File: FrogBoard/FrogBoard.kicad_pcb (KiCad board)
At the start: 2 copper layers, 59.3 x 50.6 mm, 46 parts, among them J1 Conn_01x10, J10 Conn_01x01, J11 Conn_01x01, J12 Conn_01x02, J13 Conn_01x01, J14 Conn_01x01, J15 Conn_01x01, J2 Conn_01x04, J3 USB_B_Micro, J4 Stickbox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

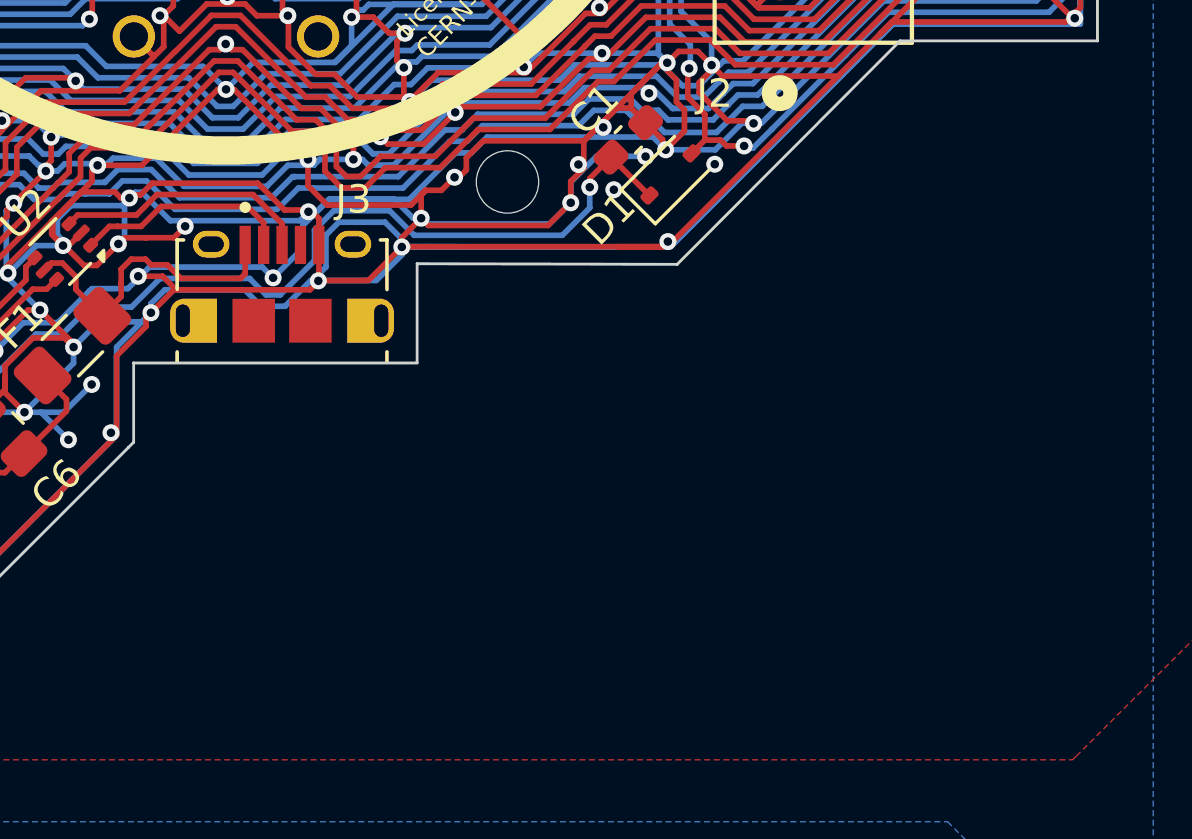
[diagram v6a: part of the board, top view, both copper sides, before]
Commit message: Replace micro B with USB-C connector
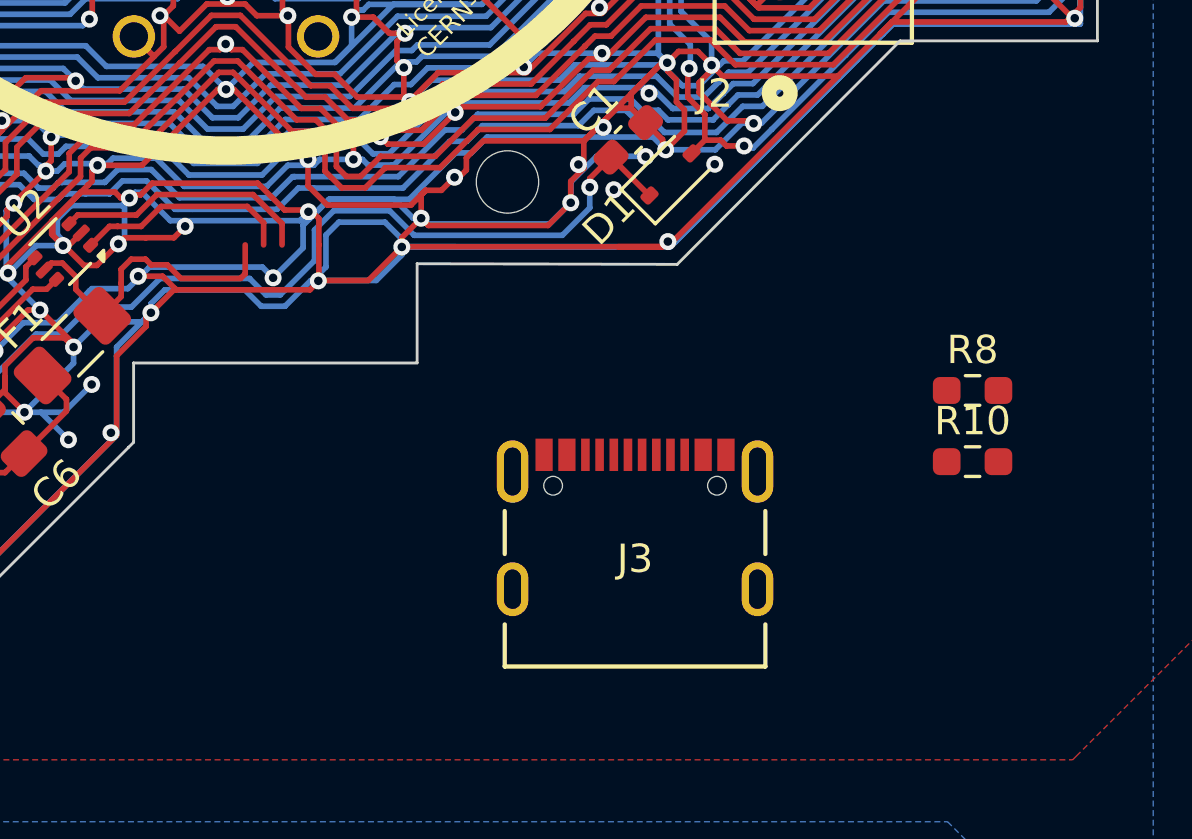
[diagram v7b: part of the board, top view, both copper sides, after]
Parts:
- added R10: 5.1k, Resistor_SMD:R_0603_1608Metric_Pad0.98x0.95mm_HandSolder, F.Cu at (178.1, 117.0)
- added R8: 5.1k, Resistor_SMD:R_0603_1608Metric_Pad0.98x0.95mm_HandSolder, F.Cu at (178.1, 114.5)
- J3: value USB_B_Micro -> USB_C_Receptacle_USB2.0_16P; footprint FrogBoard_footprints:AMPHENOL_10118194-0001LF -> FrogBoard_footprints:CONN16_C16PIN_SHN
- moved J3 15.0 mm to (166.2, 120.4)

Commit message: Cleaned up board edge positions and layed out the main bus
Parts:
- added J16: Conn_01x01, FrogBoard_footprints:FrogBoard_PinHeader_1x01_P1.00mm_Vertical, F.Cu at (21.5, 2.86)
- added J17: Conn_01x01, FrogBoard_footprints:FrogBoard_PinHeader_1x01_P1.00mm_Vertical, F.Cu at (16.8, 3.25)
- added J18: Conn_01x01, FrogBoard_footprints:FrogBoard_PinHeader_1x01_P1.00mm_Vertical, F.Cu at (18.6, 2.85)
- added J19: Conn_01x01, FrogBoard_footprints:FrogBoard_PinHeader_1x01_P1.00mm_Vertical, F.Cu at (29.2, -0.06)
- added J20: Conn_01x01, FrogBoard_footprints:FrogBoard_PinHeader_1x01_P1.00mm_Vertical, F.Cu at (28.5, 10.9)
- added J21: Conn_01x01, FrogBoard_footprints:FrogBoard_PinHeader_1x01_P1.00mm_Vertical, F.Cu at (27.2, 11.1)
- added J22: Conn_01x01, FrogBoard_footprints:FrogBoard_PinHeader_1x01_P1.00mm_Vertical, F.Cu at (25.9, 10.7)
- added J23: Conn_01x01, FrogBoard_footprints:FrogBoard_PinHeader_1x01_P1.00mm_Vertical, F.Cu at (24.5, 10.2)
- added J24: Conn_01x01, FrogBoard_footprints:FrogBoard_PinHeader_1x01_P1.00mm_Vertical, F.Cu at (23.0, 9.67)
- added J25: Conn_01x01, FrogBoard_footprints:FrogBoard_PinHeader_1x01_P1.00mm_Vertical, F.Cu at (25.2, -0.03)
- added J27: Conn_01x01, FrogBoard_footprints:FrogBoard_PinHeader_1x01_P1.00mm_Vertical, F.Cu at (20.3, 4.90)
- added J28: Conn_01x01, FrogBoard_footprints:FrogBoard_PinHeader_1x01_P1.00mm_Vertical, F.Cu at (21.6, 4.90)
- added J30: Conn_01x02, FrogBoard_footprints:PinHeader_1x02_P1.00mm_Vertical_Neutral_No_Coutryard, F.Cu at (29.8, 11.9)
- moved J3 247.0 mm to (-48.0, -2.54), turned to -90 degrees
- moved R10 245.6 mm to (-45.0, 14.4)
- moved R8 245.6 mm to (-45.0, 11.9)
- moved C4 234.2 mm to (-52.5, 56.4)
- moved J14 219.9 mm to (-57.5, 15.4)
- moved J13 214.1 mm to (-51.1, 14.7)
- moved J12 211.2 mm to (-46.7, 7.05)
- moved U1 205.4 mm to (-57.3, 37.1)
- moved J6 204.4 mm to (-54.4, 21.8)
- moved J9 203.9 mm to (-50.3, 18.5)
- moved C11 196.4 mm to (-46.3, 24.8)
- moved C8 194.5 mm to (-49.3, 31.8)
- moved J15 193.9 mm to (-40.5, 18.3)
- moved U3 193.7 mm to (-38.6, 48.1)
- moved D3 190.9 mm to (-42.6, 30.5)
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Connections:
- U4 pad 10: AX_OUT -> AY_OUT
- U4 pad 2: AY_OUT -> AX_OUT
- U4 pad 3: AY_MUX_OUT -> AX_MUX_OUT
- U4 pad 9: AX_MUX_OUT -> AY_MUX_OUT
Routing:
- net GND: track 1911.2 -> 1208.4 mm, vias 242 -> 116
- net +3.3V: track 252.0 -> 71.2 mm, vias 11 -> 2
- net AY_IN: track 94.8 -> 0.00 mm
- net AX_IN: track 77.8 -> 0.00 mm
- net STICK_BTN: track 61.0 -> 0.00 mm, vias 2 -> 0
- net +3.3V_HORI: track 35.3 -> 78.8 mm, vias 3 -> 2
- net BOOT_SEL: track 32.3 -> 0.00 mm, vias 2 -> 0
- net AX_OUT: track 63.4 -> 42.1 mm, vias 2 -> 0
- net AY_OUT: track 63.0 -> 46.1 mm, vias 2 -> 0
- net A_SEL: track 65.2 -> 48.9 mm, vias 2 -> 0
- net FFC_P2: track 57.9 -> 46.1 mm
- net VBUS: track 11.0 -> 0.00 mm
- net USB-: track 10.6 -> 0.00 mm
- net USB+: track 10.2 -> 0.00 mm
- net FFC_P5: track 66.1 -> 56.1 mm, vias 2 -> 0
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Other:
- outline, holes or cut-outs redrawn
